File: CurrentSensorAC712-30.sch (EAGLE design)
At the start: 7 parts, among them U1 ACS712ELCTR30AT

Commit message: current sensor board routed
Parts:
- added H1, H2: MOUNT-PAD-SQUARE4.3, holes:MOUNT-PAD-SQUARE4.3
- added JP3: (no value), pinhead:PINHD-1X2
- JP1: device pinhead:PINHD-1X5 -> pinhead:PINHD-1X4
- JP2: device pinhead:PINHD-1X5 -> pinhead:PINHD-1X2
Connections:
- net 5VDC: no longer JP1.2
- net GND: now also JP1.3, JP2.1, JP2.2, JP3.1, JP3.2; no longer JP1.5
- net IN: now also H1.MOUNT
- net N$6: now also JP1.2; no longer JP1.3
- net OUT: now also H2.MOUNT
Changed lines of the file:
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@@
 <layers>
 <layer number="1" name="Top" color="4" fill="1" visible="no" active="no"/>
+<layer number="2" name="Route2" color="1" fill="3" visible="no" active="no"/>
+<layer number="3" name="Route3" color="4" fill="3" visible="no" active="no"/>
+<layer number="4" name="Route4" color="1" fill="4" visible="no" active="no"/>
+<layer number="5" name="Route5" color="4" fill="4" visible="no" active="no"/>
+<layer number="6" name="Route6" color="1" fill="8" visible="no" active="no"/>
+<layer number="7" name="Route7" color="4" fill="8" visible="no" active="no"/>
+<layer number="8" name="Route8" color="1" fill="2" visible="no" active="no"/>
+<layer number="9" name="Route9" color="4" fill="2" visible="no" active="no"/>
+<layer number="10" name="Route10" color="1" fill="7" visible="no" active="no"/>
+<layer number="11" name="Route11" color="4" fill="7" visible="no" active="no"/>
+<layer number="12" name="Route12" color="1" fill="5" visible="no" active="no"/>
+<layer number="13" name="Route13" color="4" fill="5" visible="no" active="no"/>
+<layer number="14" name="Route14" color="1" fill="6" visible="no" active="no"/>
+<layer number="15" name="Route15" color="4" fill="6" visible="no" active="no"/>
 <layer number="16" name="Bottom" color="1" fill="1" visible="no" active="no"/>
 <layer number="17" name="Pads" color="2" fill="1" visible="no" active="no"/>
@@
 <part name="C2" library="rcl" library_urn="urn:adsk.eagle:library:334" deviceset="C-EU" device="C0805" package3d_urn="urn:adsk.eagle:package:23617/2" value="1nF"/>
 <part name="LED1" library="led" library_urn="urn:adsk.eagle:library:259" deviceset="LED" device="CHIPLED_0603" package3d_urn="urn:adsk.eagle:package:15822/1" value="KT-0603R"/>
-<part name="JP1" library="pinhead" library_urn="urn:adsk.eagle:library:325" deviceset="PINHD-1X5" device="" package3d_urn="urn:adsk.eagle:package:22469/2"/>
-<part name="JP2" library="pinhead" library_urn="urn:adsk.eagle:library:325" deviceset="PINHD-1X5" device="" package3d_urn="urn:adsk.eagle:package:22469/2"/>
+<part name="H1" library="holes" library_urn="urn:adsk.eagle:library:237" deviceset="MOUNT-PAD-SQUARE" device="4.3" package3d_urn="urn:adsk.eagle:package:14297/1"/>
+<part name="H2" library="holes" library_urn="urn:adsk.eagle:library:237" deviceset="MOUNT-PAD-SQUARE" device="4.3" package3d_urn="urn:adsk.eagle:package:14297/1"/>
+<part name="JP1" library="pinhead" library_urn="urn:adsk.eagle:library:325" deviceset="PINHD-1X4" device="" package3d_urn="urn:adsk.eagle:package:22407/2"/>
+<part name="JP2" library="pinhead" library_urn="urn:adsk.eagle:library:325" deviceset="PINHD-1X2" device="" package3d_urn="urn:adsk.eagle:package:22435/2"/>
+<part name="JP3" library="pinhead" library_urn="urn:adsk.eagle:library:325" deviceset="PINHD-1X2" device="" package3d_urn="urn:adsk.eagle:package:22435/2"/>
 </parts>
 <sheets>
@@
 <attribute name="VALUE" x="134.112" y="90.805" size="1.778" layer="96" rot="R180"/>
 </instance>
-<instance part="JP1" gate="A" x="185.42" y="64.77" smashed="yes">
-<attribute name="NAME" x="179.07" y="73.025" size="1.778" layer="95"/>
+<instance part="H1" gate="G$1" x="27.94" y="72.39" smashed="yes" rot="R180">
+<attribute name="NAME" x="25.146" y="71.8058" size="1.778" layer="95" rot="R180"/>
+<attribute name="VALUE" x="25.146" y="74.8538" size="1.778" layer="96" rot="R180"/>
+</instance>
+<instance part="H2" gate="G$1" x="27.94" y="52.07" smashed="yes" rot="R180">
+<attribute name="NAME" x="25.146" y="51.4858" size="1.778" layer="95" rot="R180"/>
+<attribute name="VALUE" x="25.146" y="54.5338" size="1.778" layer="96" rot="R180"/>
+</instance>
+<instance part="JP1" gate="A" x="185.42" y="62.23" smashed="yes">
+<attribute name="NAME" x="179.07" y="70.485" size="1.778" layer="95"/>
 <attribute name="VALUE" x="179.07" y="54.61" size="1.778" layer="96"/>
 </instance>
-<instance part="JP2" gate="A" x="185.42" y="44.45" smashed="yes">
-<attribute name="NAME" x="179.07" y="52.705" size="1.778" layer="95"/>
+<instance part="JP2" gate="G$1" x="185.42" y="39.37" smashed="yes">
+<attribute name="NAME" x="179.07" y="45.085" size="1.778" layer="95"/>
 <attribute name="VALUE" x="179.07" y="34.29" size="1.778" layer="96"/>
+</instance>
+<instance part="JP3" gate="G$1" x="185.42" y="49.53" smashed="yes">
+<attribute name="NAME" x="179.07" y="55.245" size="1.778" layer="95"/>
+<attribute name="VALUE" x="179.07" y="44.45" size="1.778" layer="96"/>
 </instance>
 </instances>
@@
 <wire x1="67.31" y1="72.39" x2="30.48" y2="72.39" width="0.1524" layer="91"/>
 <label x="45.72" y="74.93" size="1.778" layer="95"/>
+<pinref part="H1" gate="G$1" pin="MOUNT"/>
 </segment>
 </net>
@@
 <wire x1="67.31" y1="52.07" x2="30.48" y2="52.07" width="0.1524" layer="91"/>
 <label x="46.99" y="49.53" size="1.778" layer="95"/>
+<pinref part="H2" gate="G$1" pin="MOUNT"/>
 </segment>
 </net>
@@
 <junction x="152.4" y="102.87"/>
 <label x="129.54" y="106.68" size="1.778" layer="95"/>
-<pinref part="JP1" gate="A" pin="2"/>
 <pinref part="JP1" gate="A" pin="1"/>
-<wire x1="182.88" y1="67.31" x2="182.88" y2="69.85" width="0.1524" layer="91"/>
-<junction x="182.88" y="67.31"/>
 </segment>
 </net>
@@
 <junction x="121.92" y="40.64"/>
 <wire x1="181.61" y1="59.69" x2="181.61" y2="62.23" width="0.1524" layer="91"/>
-<pinref part="JP1" gate="A" pin="5"/>
-<wire x1="181.61" y1="59.69" x2="182.88" y2="59.69" width="0.1524" layer="91"/>
-<pinref part="JP1" gate="A" pin="4"/>
 <wire x1="182.88" y1="62.23" x2="181.61" y2="62.23" width="0.1524" layer="91"/>
 <junction x="181.61" y="62.23"/>
+<pinref part="JP1" gate="A" pin="3"/>
+<pinref part="JP1" gate="A" pin="4"/>
+<wire x1="181.61" y1="59.69" x2="182.88" y2="59.69" width="0.1524" layer="91"/>
+<wire x1="181.61" y1="59.69" x2="181.61" y2="52.07" width="0.1524" layer="91"/>
+<junction x="181.61" y="59.69"/>
+<pinref part="JP2" gate="G$1" pin="2"/>
+<wire x1="181.61" y1="52.07" x2="181.61" y2="49.53" width="0.1524" layer="91"/>
+<wire x1="181.61" y1="49.53" x2="181.61" y2="41.91" width="0.1524" layer="91"/>
+<wire x1="181.61" y1="41.91" x2="181.61" y2="39.37" width="0.1524" layer="91"/>
+<wire x1="181.61" y1="39.37" x2="182.88" y2="39.37" width="0.1524" layer="91"/>
+<pinref part="JP3" gate="G$1" pin="1"/>
+<wire x1="181.61" y1="52.07" x2="182.88" y2="52.07" width="0.1524" layer="91"/>
+<junction x="181.61" y="52.07"/>
+<pinref part="JP3" gate="G$1" pin="2"/>
+<wire x1="181.61" y1="49.53" x2="182.88" y2="49.53" width="0.1524" layer="91"/>
+<junction x="181.61" y="49.53"/>
+<pinref part="JP2" gate="G$1" pin="1"/>
+<wire x1="181.61" y1="41.91" x2="182.88" y2="41.91" width="0.1524" layer="91"/>
+<junction x="181.61" y="41.91"/>
 </segment>
 </net>
@@
 <pinref part="U1" gate="G$1" pin="VIOUT"/>
 <wire x1="102.87" y1="64.77" x2="182.88" y2="64.77" width="0.1524" layer="91"/>
-<pinref part="JP1" gate="A" pin="3"/>
-</segment>
-</net>
+<pinref part="JP1" gate="A" pin="2"/>
+</segment>
+</net>

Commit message: sensor changed to ACS758
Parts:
- removed C2: 1nF, rcl:C-EUC0805
- removed U1: ACS712ELCTR30AT, ACS712ELCTR30AT:ACS712ELCTR30AT
- added IC1: ACS758LCB-050B-PFF-T, allegro-2:ACS758LCB-050B-PFF-T
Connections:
- removed net N$4: C2.1, U1.FILTER
- net 5VDC: now also IC1.VCC; no longer U1.VCC
- net GND: now also IC1.GND; no longer C2.2, U1.GND
- net IN: now also IC1.IP+; no longer U1.IP+
- net N$6: now also IC1.VOUT; no longer U1.VIOUT
- net OUT: now also IC1.IP-; no longer U1.IP-

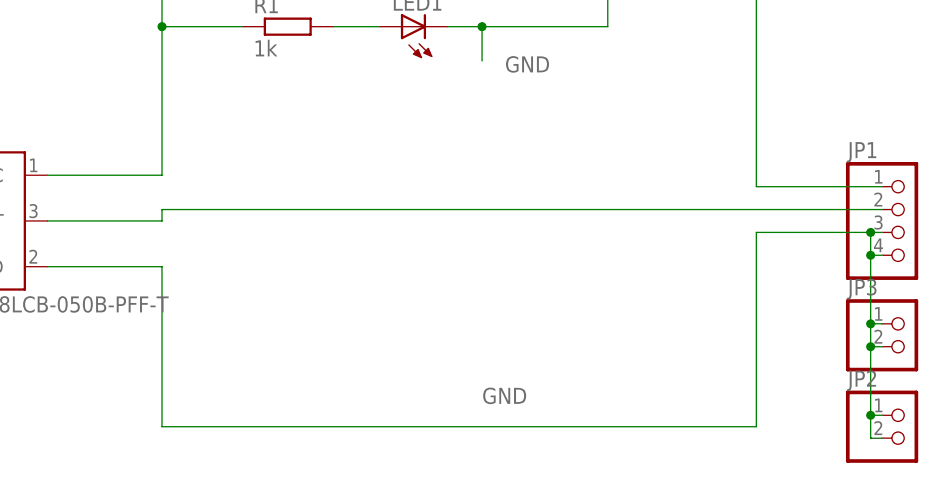
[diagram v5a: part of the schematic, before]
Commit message: sensor ACS758 layouted
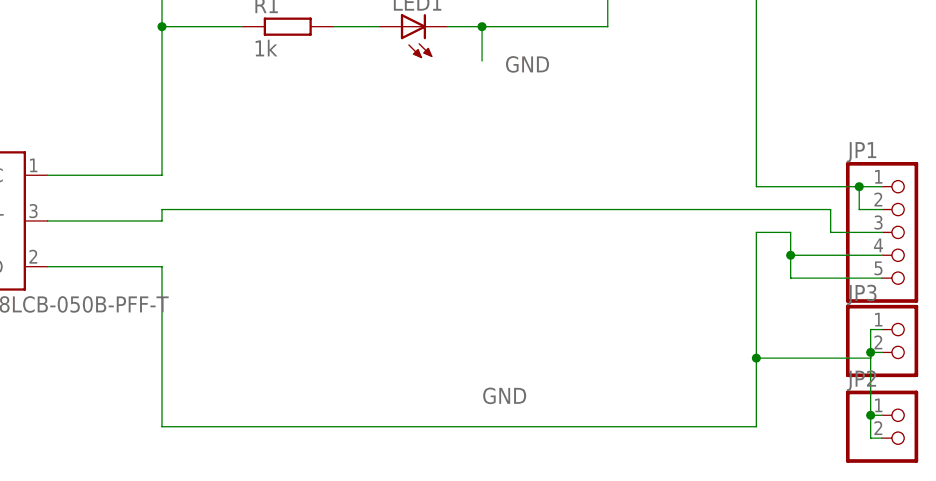
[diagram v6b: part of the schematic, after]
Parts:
- JP1: device pinhead:PINHD-1X4 -> pinhead:PINHD-1X5
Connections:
- net 5VDC: now also JP1.2
- net GND: now also JP1.5; no longer JP1.3
- net N$6: now also JP1.3; no longer JP1.2
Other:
- moved on the sheet: JP3
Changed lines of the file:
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@@
 <setting verticaltext="up"/>
 </settings>
-<grid distance="50" unitdist="mil" unit="mil" style="lines" multiple="1" display="yes" altdistance="0.01" altunitdist="inch" altunit="inch"/>
+<grid distance="25" unitdist="mil" unit="mil" style="lines" multiple="1" display="yes" altdistance="0.01" altunitdist="inch" altunit="inch"/>
 <layers>
 <layer number="1" name="Top" color="4" fill="1" visible="no" active="no"/>
@@
 <part name="H1" library="holes" library_urn="urn:adsk.eagle:library:237" deviceset="MOUNT-PAD-SQUARE" device="4.3" package3d_urn="urn:adsk.eagle:package:14297/1"/>
 <part name="H2" library="holes" library_urn="urn:adsk.eagle:library:237" deviceset="MOUNT-PAD-SQUARE" device="4.3" package3d_urn="urn:adsk.eagle:package:14297/1"/>
-<part name="JP1" library="pinhead" library_urn="urn:adsk.eagle:library:325" deviceset="PINHD-1X4" device="" package3d_urn="urn:adsk.eagle:package:22407/2"/>
+<part name="JP1" library="pinhead" library_urn="urn:adsk.eagle:library:325" deviceset="PINHD-1X5" device="" package3d_urn="urn:adsk.eagle:package:22469/2"/>
 <part name="JP2" library="pinhead" library_urn="urn:adsk.eagle:library:325" deviceset="PINHD-1X2" device="" package3d_urn="urn:adsk.eagle:package:22435/2"/>
 <part name="JP3" library="pinhead" library_urn="urn:adsk.eagle:library:325" deviceset="PINHD-1X2" device="" package3d_urn="urn:adsk.eagle:package:22435/2"/>
@@
 <attribute name="VALUE" x="179.07" y="34.29" size="1.778" layer="96"/>
 </instance>
-<instance part="JP3" gate="G$1" x="185.42" y="49.53" smashed="yes">
-<attribute name="NAME" x="179.07" y="55.245" size="1.778" layer="95"/>
-<attribute name="VALUE" x="179.07" y="44.45" size="1.778" layer="96"/>
+<instance part="JP3" gate="G$1" x="185.42" y="48.895" smashed="yes">
+<attribute name="NAME" x="179.07" y="54.61" size="1.778" layer="95"/>
+<attribute name="VALUE" x="179.07" y="43.815" size="1.778" layer="96"/>
 </instance>
 <instance part="IC1" gate="G$1" x="80.01" y="63.5" smashed="yes">
@@
 <net name="5VDC" class="0">
 <segment>
-<wire x1="182.88" y1="67.31" x2="168.91" y2="67.31" width="0.1524" layer="91"/>
+<wire x1="182.88" y1="67.31" x2="180.34" y2="67.31" width="0.1524" layer="91"/>
+<wire x1="180.34" y1="67.31" x2="168.91" y2="67.31" width="0.1524" layer="91"/>
 <wire x1="168.91" y1="67.31" x2="168.91" y2="102.87" width="0.1524" layer="91"/>
 <wire x1="168.91" y1="102.87" x2="152.4" y2="102.87" width="0.1524" layer="91"/>
@@
 <pinref part="IC1" gate="G$1" pin="VCC"/>
 <wire x1="90.17" y1="68.58" x2="102.87" y2="68.58" width="0.1524" layer="91"/>
+<pinref part="JP1" gate="A" pin="2"/>
+<wire x1="182.88" y1="64.77" x2="180.34" y2="64.77" width="0.1524" layer="91"/>
+<wire x1="180.34" y1="64.77" x2="180.34" y2="67.31" width="0.1524" layer="91"/>
+<junction x="180.34" y="67.31"/>
 </segment>
 </net>
@@
 </segment>
 <segment>
-<wire x1="181.61" y1="62.23" x2="168.91" y2="62.23" width="0.1524" layer="91"/>
-<wire x1="168.91" y1="62.23" x2="168.91" y2="40.64" width="0.1524" layer="91"/>
+<wire x1="168.91" y1="62.23" x2="168.91" y2="48.26" width="0.1524" layer="91"/>
+<wire x1="168.91" y1="48.26" x2="168.91" y2="40.64" width="0.1524" layer="91"/>
 <wire x1="168.91" y1="40.64" x2="102.87" y2="40.64" width="0.1524" layer="91"/>
 <wire x1="102.87" y1="40.64" x2="102.87" y2="58.42" width="0.1524" layer="91"/>
 <label x="138.43" y="43.18" size="1.778" layer="95"/>
-<wire x1="181.61" y1="59.69" x2="181.61" y2="62.23" width="0.1524" layer="91"/>
-<wire x1="182.88" y1="62.23" x2="181.61" y2="62.23" width="0.1524" layer="91"/>
-<junction x="181.61" y="62.23"/>
-<pinref part="JP1" gate="A" pin="3"/>
+<pinref part="IC1" gate="G$1" pin="GND"/>
+<wire x1="90.17" y1="58.42" x2="102.87" y2="58.42" width="0.1524" layer="91"/>
+<wire x1="168.91" y1="62.23" x2="172.72" y2="62.23" width="0.1524" layer="91"/>
+<wire x1="172.72" y1="62.23" x2="172.72" y2="59.69" width="0.1524" layer="91"/>
+<pinref part="JP1" gate="A" pin="5"/>
+<wire x1="172.72" y1="59.69" x2="172.72" y2="57.15" width="0.1524" layer="91"/>
+<wire x1="172.72" y1="57.15" x2="182.88" y2="57.15" width="0.1524" layer="91"/>
 <pinref part="JP1" gate="A" pin="4"/>
-<wire x1="181.61" y1="59.69" x2="182.88" y2="59.69" width="0.1524" layer="91"/>
-<wire x1="181.61" y1="59.69" x2="181.61" y2="52.07" width="0.1524" layer="91"/>
-<junction x="181.61" y="59.69"/>
+<wire x1="182.88" y1="59.69" x2="172.72" y2="59.69" width="0.1524" layer="91"/>
+<junction x="172.72" y="59.69"/>
 <pinref part="JP2" gate="G$1" pin="2"/>
-<wire x1="181.61" y1="52.07" x2="181.61" y2="49.53" width="0.1524" layer="91"/>
-<wire x1="181.61" y1="49.53" x2="181.61" y2="41.91" width="0.1524" layer="91"/>
+<pinref part="JP2" gate="G$1" pin="1"/>
+<pinref part="JP3" gate="G$1" pin="2"/>
+<pinref part="JP3" gate="G$1" pin="1"/>
+<wire x1="181.61" y1="51.435" x2="182.88" y2="51.435" width="0.1524" layer="91"/>
+<wire x1="181.61" y1="51.435" x2="181.61" y2="48.895" width="0.1524" layer="91"/>
+<wire x1="181.61" y1="48.895" x2="182.88" y2="48.895" width="0.1524" layer="91"/>
+<junction x="181.61" y="48.895"/>
+<wire x1="181.61" y1="48.895" x2="181.61" y2="41.91" width="0.1524" layer="91"/>
+<wire x1="181.61" y1="41.91" x2="182.88" y2="41.91" width="0.1524" layer="91"/>
+<junction x="181.61" y="41.91"/>
 <wire x1="181.61" y1="41.91" x2="181.61" y2="39.37" width="0.1524" layer="91"/>
 <wire x1="181.61" y1="39.37" x2="182.88" y2="39.37" width="0.1524" layer="91"/>
-<pinref part="JP3" gate="G$1" pin="1"/>
-<wire x1="181.61" y1="52.07" x2="182.88" y2="52.07" width="0.1524" layer="91"/>
-<junction x="181.61" y="52.07"/>
-<pinref part="JP3" gate="G$1" pin="2"/>
-<wire x1="181.61" y1="49.53" x2="182.88" y2="49.53" width="0.1524" layer="91"/>
-<junction x="181.61" y="49.53"/>
-<pinref part="JP2" gate="G$1" pin="1"/>
-<wire x1="181.61" y1="41.91" x2="182.88" y2="41.91" width="0.1524" layer="91"/>
-<junction x="181.61" y="41.91"/>
-<pinref part="IC1" gate="G$1" pin="GND"/>
-<wire x1="90.17" y1="58.42" x2="102.87" y2="58.42" width="0.1524" layer="91"/>
+<wire x1="181.61" y1="48.895" x2="181.61" y2="48.26" width="0.1524" layer="91"/>
+<wire x1="181.61" y1="48.26" x2="168.91" y2="48.26" width="0.1524" layer="91"/>
+<junction x="168.91" y="48.26"/>
 </segment>
 </net>
 <net name="N$6" class="0">
 <segment>
-<wire x1="102.87" y1="64.77" x2="182.88" y2="64.77" width="0.1524" layer="91"/>
-<pinref part="JP1" gate="A" pin="2"/>
 <pinref part="IC1" gate="G$1" pin="VOUT"/>
 <wire x1="90.17" y1="63.5" x2="102.87" y2="63.5" width="0.1524" layer="91"/>
 <wire x1="102.87" y1="63.5" x2="102.87" y2="64.77" width="0.1524" layer="91"/>
-</segment>
-</net>
+<pinref part="JP1" gate="A" pin="3"/>
+<wire x1="182.88" y1="62.23" x2="177.165" y2="62.23" width="0.1524" layer="91"/>
+<wire x1="177.165" y1="62.23" x2="177.165" y2="64.77" width="0.1524" layer="91"/>
+<wire x1="177.165" y1="64.77" x2="102.87" y2="64.77" width="0.1524" layer="91"/>
+</segment>
+</net>

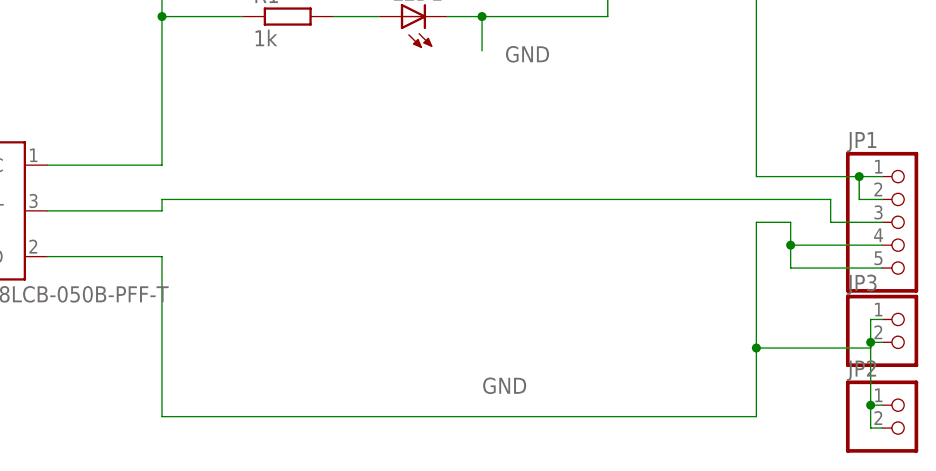
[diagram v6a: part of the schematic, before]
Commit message: new footprint for current sensor added
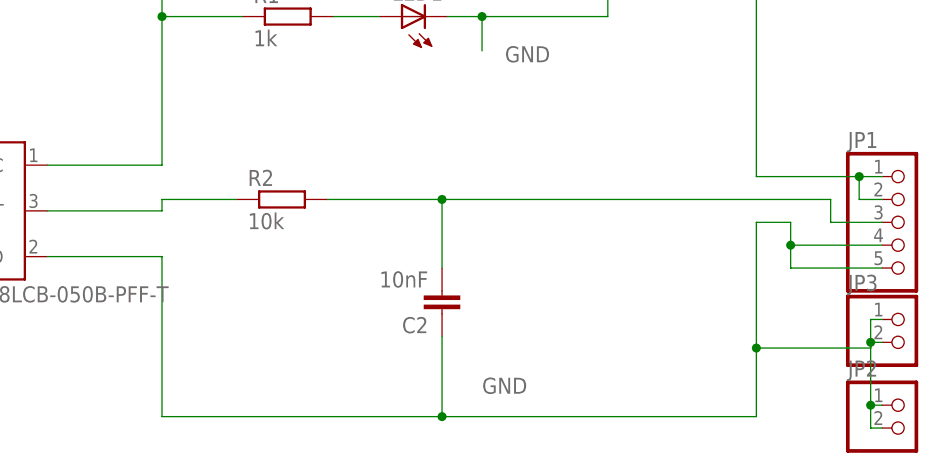
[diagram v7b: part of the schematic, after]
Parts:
- added C2: 10nF, rcl:C-EUC0805
- added R2: 10k, rcl:R-EU_R0805
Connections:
- new net N$1: IC1.VOUT, R2.1
- net GND: now also C2.1
- net N$6: now also C2.2, R2.2; no longer IC1.VOUT
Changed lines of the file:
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@@
 <part name="JP3" library="pinhead" library_urn="urn:adsk.eagle:library:325" deviceset="PINHD-1X2" device="" package3d_urn="urn:adsk.eagle:package:22435/2"/>
 <part name="IC1" library="allegro-2" deviceset="ACS758*" device="" technology="LCB-050B-PFF-T"/>
+<part name="R2" library="rcl" library_urn="urn:adsk.eagle:library:334" deviceset="R-EU_" device="R0805" package3d_urn="urn:adsk.eagle:package:23553/2" value="10k"/>
+<part name="C2" library="rcl" library_urn="urn:adsk.eagle:library:334" deviceset="C-EU" device="C0805" package3d_urn="urn:adsk.eagle:package:23617/2" value="10nF"/>
 </parts>
 <sheets>
@@
 <attribute name="NAME" x="77.47" y="72.39" size="1.778" layer="95"/>
 <attribute name="VALUE" x="77.47" y="53.34" size="1.778" layer="96"/>
+</instance>
+<instance part="R2" gate="G$1" x="116.205" y="64.77" smashed="yes">
+<attribute name="NAME" x="112.395" y="66.2686" size="1.778" layer="95"/>
+<attribute name="VALUE" x="112.395" y="61.468" size="1.778" layer="96"/>
+</instance>
+<instance part="C2" gate="G$1" x="133.985" y="52.07" smashed="yes" rot="R180">
+<attribute name="NAME" x="132.461" y="51.689" size="1.778" layer="95" rot="R180"/>
+<attribute name="VALUE" x="132.461" y="56.769" size="1.778" layer="96" rot="R180"/>
 </instance>
 </instances>
@@
 <wire x1="168.91" y1="62.23" x2="168.91" y2="48.26" width="0.1524" layer="91"/>
 <wire x1="168.91" y1="48.26" x2="168.91" y2="40.64" width="0.1524" layer="91"/>
-<wire x1="168.91" y1="40.64" x2="102.87" y2="40.64" width="0.1524" layer="91"/>
+<wire x1="168.91" y1="40.64" x2="133.985" y2="40.64" width="0.1524" layer="91"/>
+<wire x1="133.985" y1="40.64" x2="102.87" y2="40.64" width="0.1524" layer="91"/>
 <wire x1="102.87" y1="40.64" x2="102.87" y2="58.42" width="0.1524" layer="91"/>
 <label x="138.43" y="43.18" size="1.778" layer="95"/>
@@
 <wire x1="181.61" y1="48.26" x2="168.91" y2="48.26" width="0.1524" layer="91"/>
 <junction x="168.91" y="48.26"/>
+<pinref part="C2" gate="G$1" pin="1"/>
+<wire x1="133.985" y1="49.53" x2="133.985" y2="40.64" width="0.1524" layer="91"/>
+<junction x="133.985" y="40.64"/>
 </segment>
 </net>
 <net name="N$6" class="0">
 <segment>
-<pinref part="IC1" gate="G$1" pin="VOUT"/>
-<wire x1="90.17" y1="63.5" x2="102.87" y2="63.5" width="0.1524" layer="91"/>
-<wire x1="102.87" y1="63.5" x2="102.87" y2="64.77" width="0.1524" layer="91"/>
 <pinref part="JP1" gate="A" pin="3"/>
 <wire x1="182.88" y1="62.23" x2="177.165" y2="62.23" width="0.1524" layer="91"/>
 <wire x1="177.165" y1="62.23" x2="177.165" y2="64.77" width="0.1524" layer="91"/>
-<wire x1="177.165" y1="64.77" x2="102.87" y2="64.77" width="0.1524" layer="91"/>
+<wire x1="177.165" y1="64.77" x2="133.985" y2="64.77" width="0.1524" layer="91"/>
+<pinref part="R2" gate="G$1" pin="2"/>
+<pinref part="C2" gate="G$1" pin="2"/>
+<wire x1="133.985" y1="64.77" x2="121.285" y2="64.77" width="0.1524" layer="91"/>
+<wire x1="133.985" y1="57.15" x2="133.985" y2="64.77" width="0.1524" layer="91"/>
+<junction x="133.985" y="64.77"/>
 </segment>
 </net>
+<net name="N$1" class="0">
+<segment>
+<wire x1="111.125" y1="64.77" x2="102.87" y2="64.77" width="0.1524" layer="91"/>
+<wire x1="102.87" y1="63.5" x2="102.87" y2="64.77" width="0.1524" layer="91"/>
+<pinref part="IC1" gate="G$1" pin="VOUT"/>
+<wire x1="90.17" y1="63.5" x2="102.87" y2="63.5" width="0.1524" layer="91"/>
+<pinref part="R2" gate="G$1" pin="1"/>
+</segment>
+</net>
